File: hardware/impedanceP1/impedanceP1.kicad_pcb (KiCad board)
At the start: 2 copper layers, 53.5 x 41 mm, 35 parts, among them J1 RJ45, J2 RJ45, U1 CD4067, U2 CD4067, U3 AD5280, U4 LM234

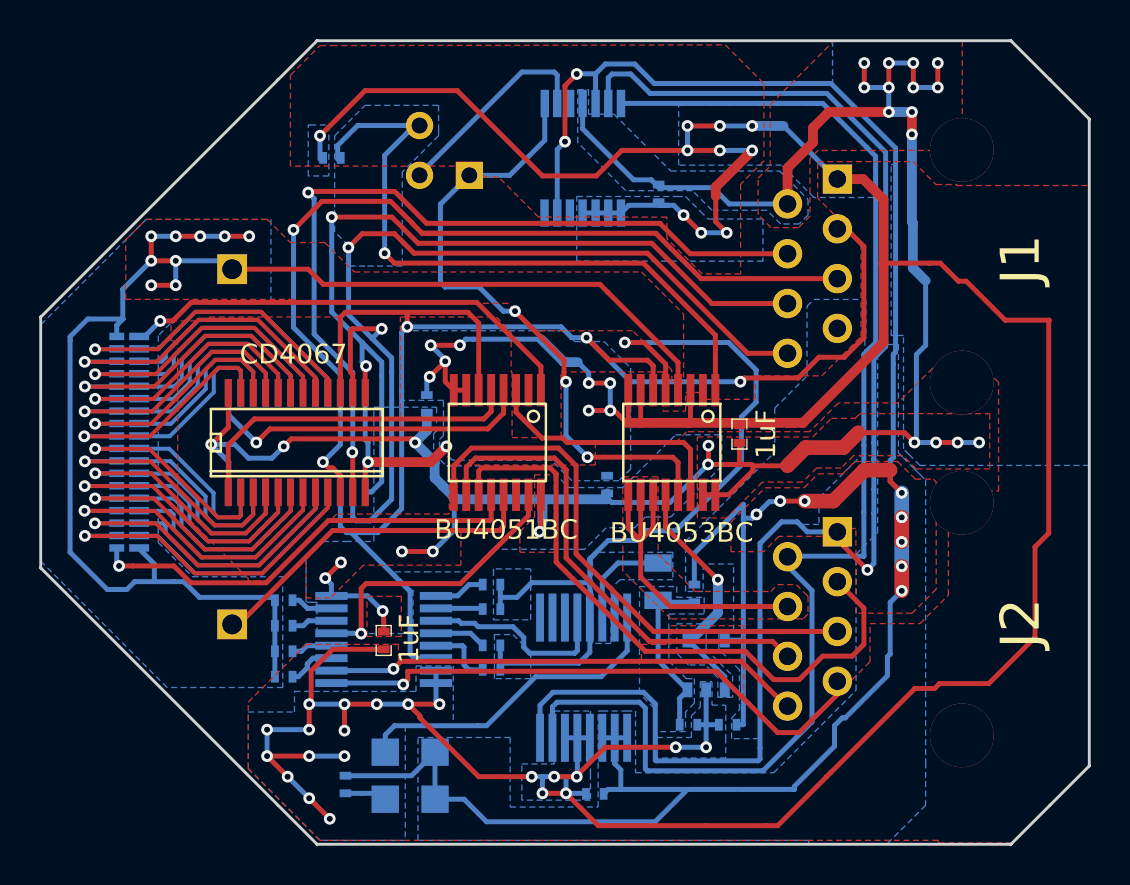
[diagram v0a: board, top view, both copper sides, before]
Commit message: updated to kicad 5 and clean up
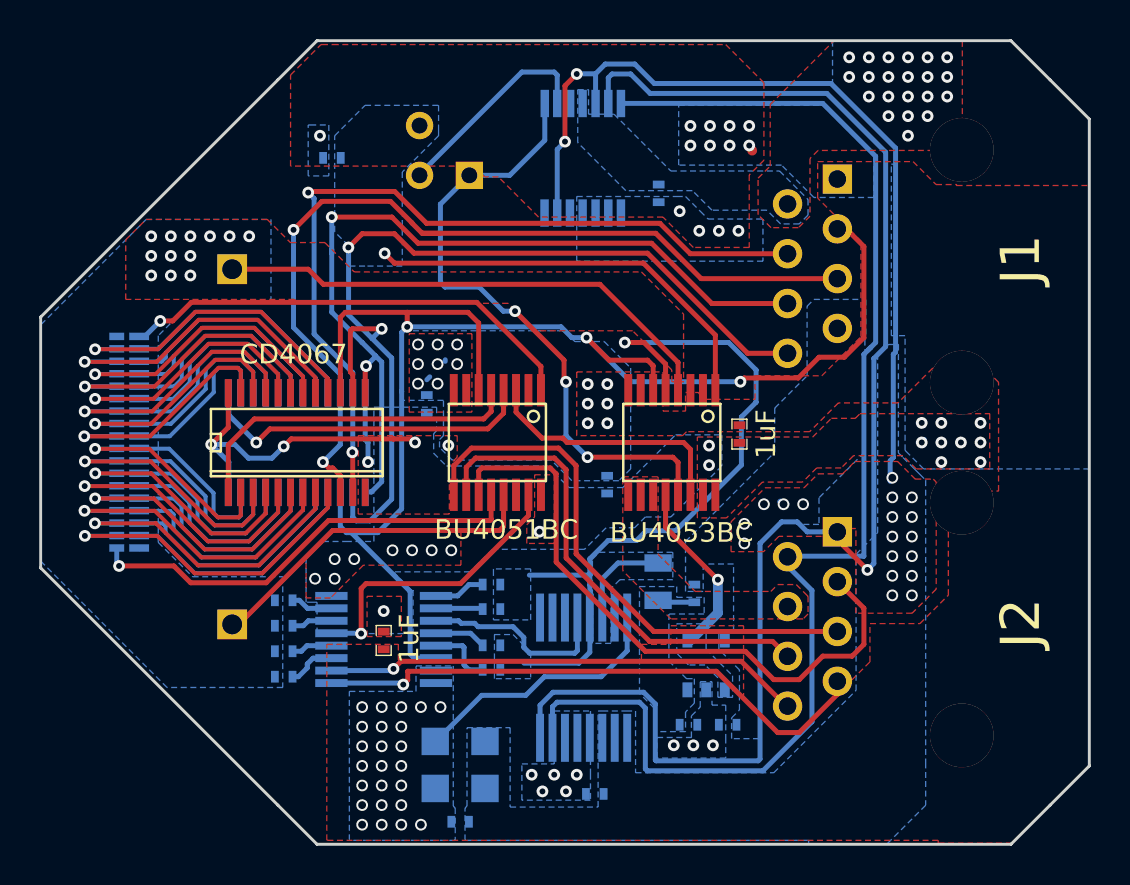
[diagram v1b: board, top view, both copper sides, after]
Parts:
- moved C8 6.15 mm to (196.4, 169.3), turned to 0 degrees
- moved OSC1 2.61 mm to (196.4, 166.4)
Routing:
- net GND: track 224.5 -> 4.34 mm, vias 41 -> 61
- net /10VOUT: track 122.1 -> 17.6 mm, vias 26 -> 45
- net /5VOUT: track 125.8 -> 44.4 mm, vias 10 -> 20
- net /EIBGND: track 75.6 -> 26.8 mm, vias 9 -> 12
- net /X2V10: track 17.6 -> 0.00 mm
- net /CURPWR: track 34.1 -> 21.7 mm
- net /TOUTAMP: track 9.02 -> 1.92 mm
- net /TESTIN: track 43.1 -> 37.5 mm
- net /TESTOUT: track 12.8 -> 9.29 mm
- net N-0000029: track 16.7 -> 13.4 mm
- net /X16S3V10: track 43.6 -> 43.0 mm
